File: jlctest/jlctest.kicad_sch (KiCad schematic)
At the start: 44 parts, among them Q1 MMBT5551, Q2 S8550, Q3 SI2301CDS, Q4 AO3401A, Q5 D882, SW1 TS-1187A-B-A-B, U1 OP07CDR, U10 L78M05, U2 TPS5430DDAR, U3 SP485EEN, U4 W25Q128JVSIQTR, U5 LM324DT, U6 74HC595, U7 SP3232EEY, U8 AMS1117-3.3, U9 AMS1117-5.0, X1 16MHz, X2 32.768kHz, X3 12MHz, X4 8MHz, X5 8MHz

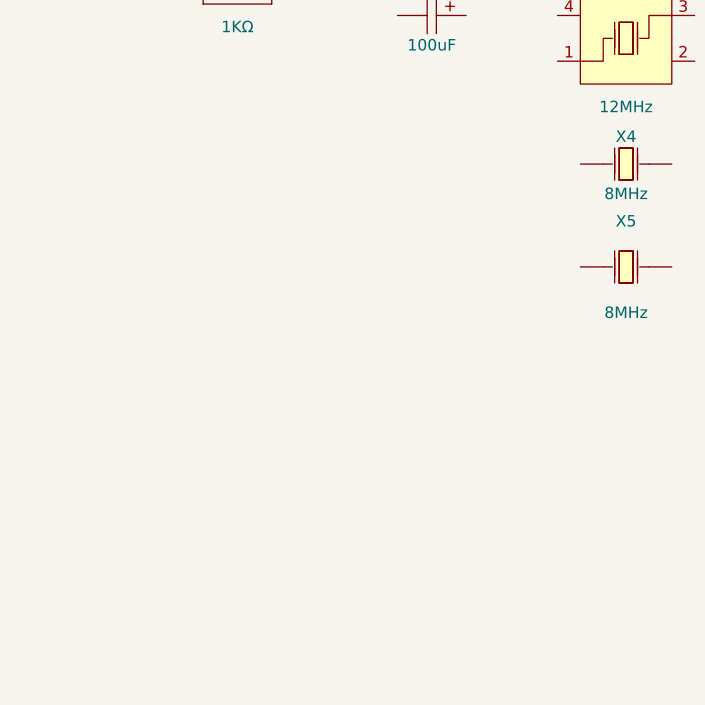
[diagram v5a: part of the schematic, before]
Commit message: Replaced missing footprints for dual op-amps
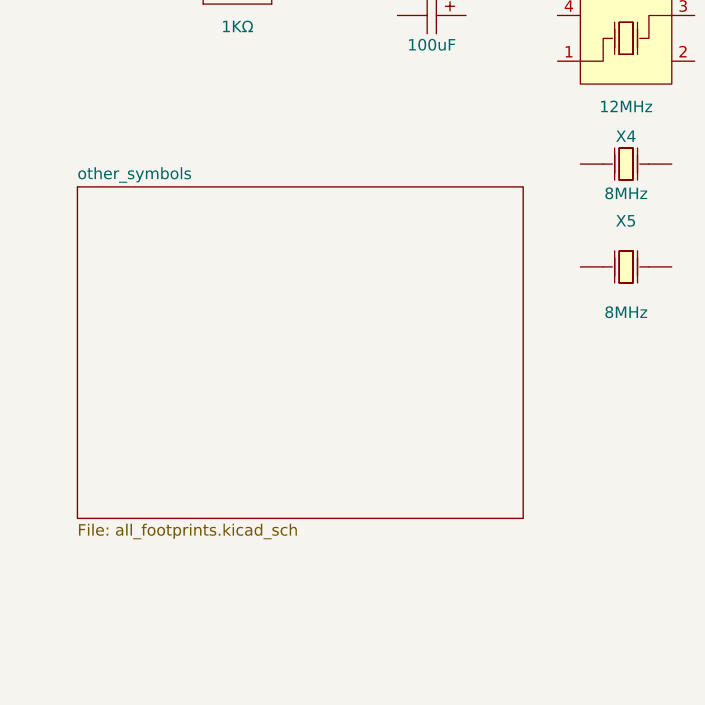
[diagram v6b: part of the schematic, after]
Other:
- added sheet other_symbols (all_footprints.kicad_sch)
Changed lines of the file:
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@@
+		)
+	)
+	(sheet
+		(at 26.67 135.89)
+		(size 49.53 36.83)
+		(exclude_from_sim no)
+		(in_bom yes)
+		(on_board yes)
+		(dnp no)
+		(fields_autoplaced yes)
+		(stroke
+			(width 0.1524)
+			(type solid)
+		)
+		(fill
+			(color 0 0 0 0.0000)
+		)
+		(property "Sheetname" "other_symbols"
+			(at 26.67 135.1784 0)
+			(effects
+				(font
+					(size 1.27 1.27)
+				)
+				(justify left bottom)
+			)
+		)
+		(property "Sheetfile" "all_footprints.kicad_sch"
+			(at 26.67 173.3046 0)
+			(effects
+				(font
+					(size 1.27 1.27)
+				)
+				(justify left top)
+			)
+		)
+		(instances
+			(project "jlctest"
+				(path "/244c2a7a-0b90-4473-b14c-9608fe251070"
+					(page "2")
+				)
+			)
 		)
 	)

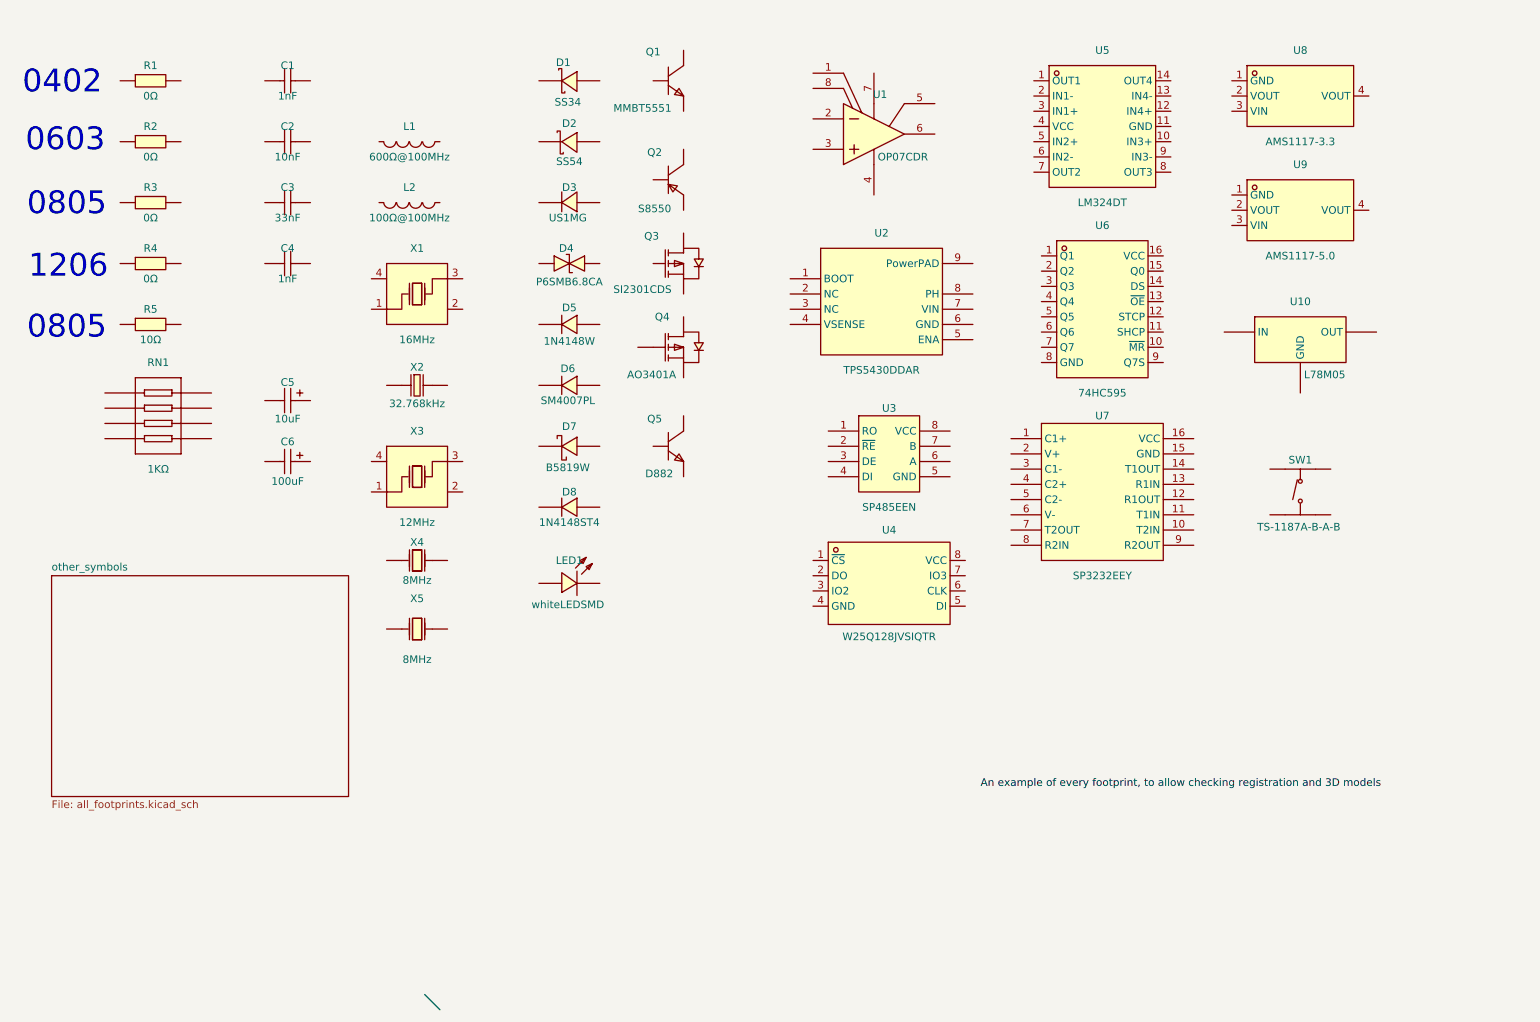
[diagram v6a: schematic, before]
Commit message: Used (extends) on all symbols having an identical set of child symbols
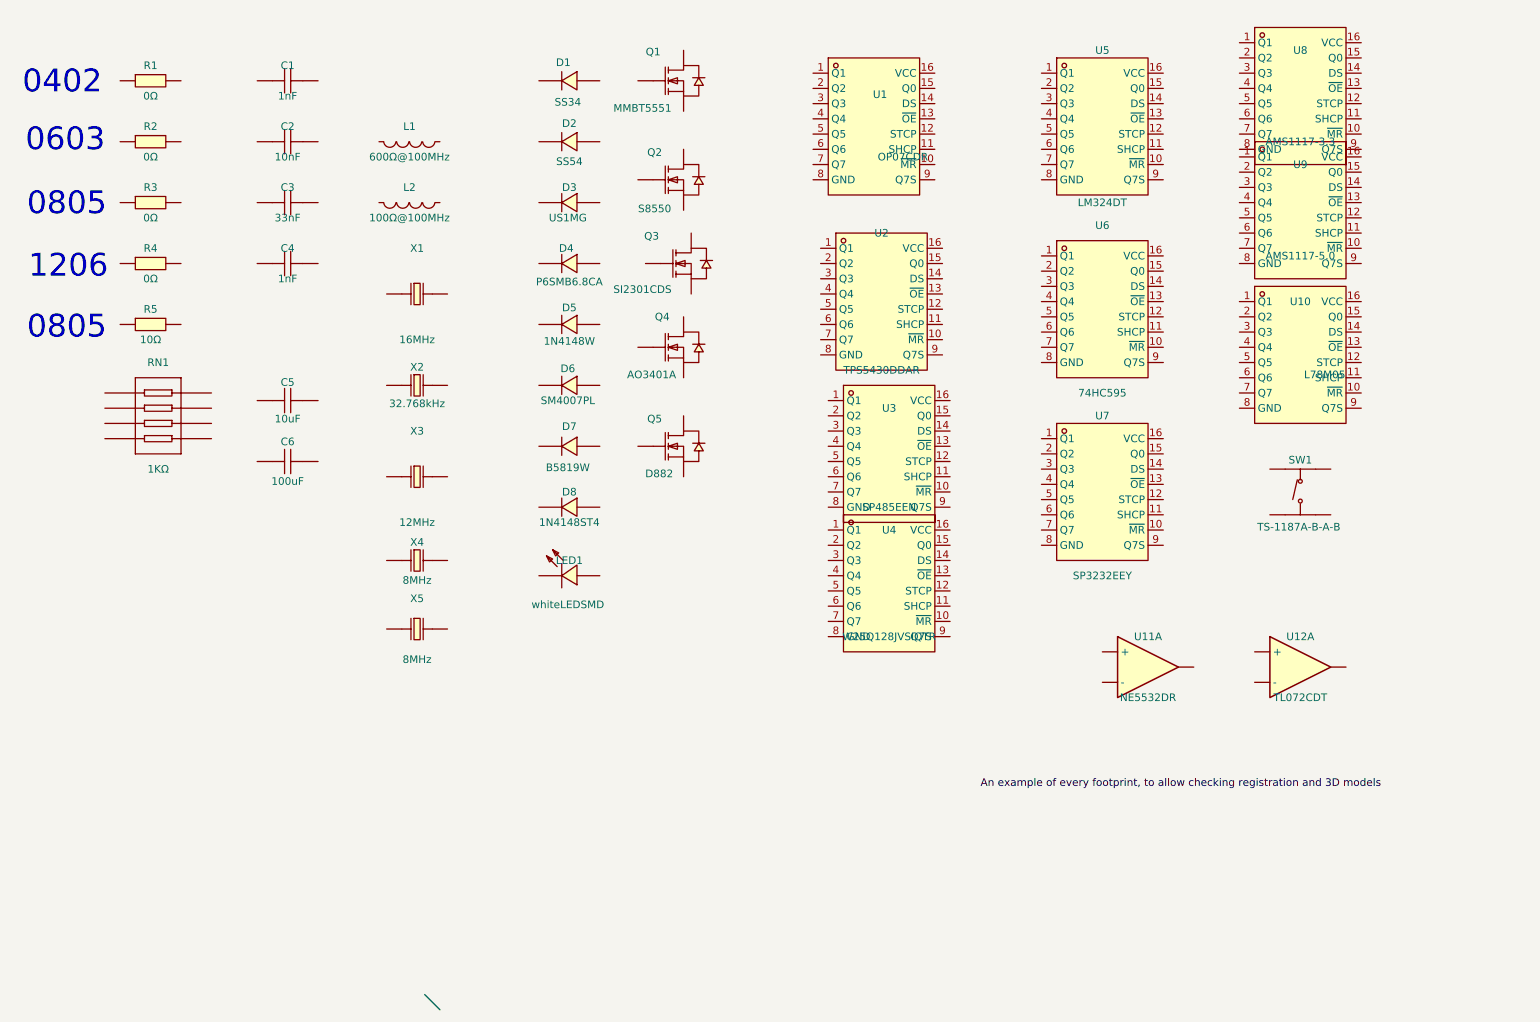
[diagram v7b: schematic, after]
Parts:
- added U11: NE5532DR, jlcbasic:SOIC-8_L4.9-W3.9-P1.27-LS6.0-BL, symbol jlcbasic:NE5532
- added U12: TL072CDT, jlcbasic:SOIC-8_L5.0-W4.0-P1.27-LS6.0-BL, symbol jlcbasic:TL072
- C1: PartNumber 1nF-0402 -> 0402B102K500NT
- C2: PartNumber 10nF-0603 -> 0603B103K500NT
- C3: PartNumber 33nF-0805 -> 0805B333K500NT
- C4: PartNumber 1nF-1206 -> 1206B102K202NT
- L1: PartNumber 600Ω@100MHz-0603 -> GZ1608D601TF
- L2: PartNumber 100Ω@100MHz-0805 -> GZ2012D101TF
- R1: PartNumber 0Ω-0402 -> 0402WGF0000TCE
- R2: PartNumber 0Ω-0603 -> 0603WAF0000T5E
- R3: PartNumber 0Ω-0805 -> 0805W8F0000T5E
- R4: PartNumber 0Ω-1206 -> 1206W4F0000T5E
- R5: PartNumber 10Ω-0805 -> 0805W8F100JT5E
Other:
- removed sheet other_symbols
- moved on the sheet: LED1
